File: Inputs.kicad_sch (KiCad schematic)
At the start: 5 parts, among them J401 inputs, J402 inputs, J403 common, U401 MCP23017_SP

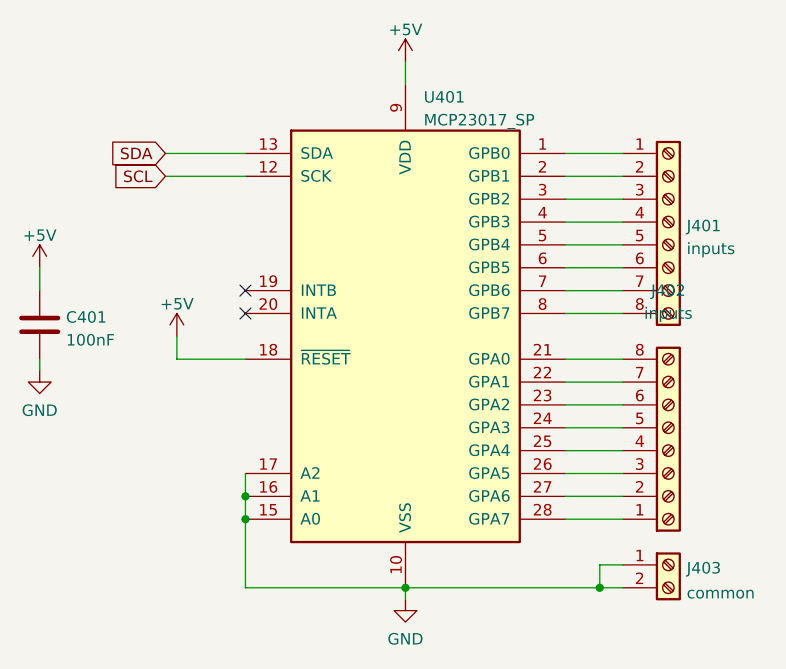
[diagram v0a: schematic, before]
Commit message: added something to debug the channel buttons
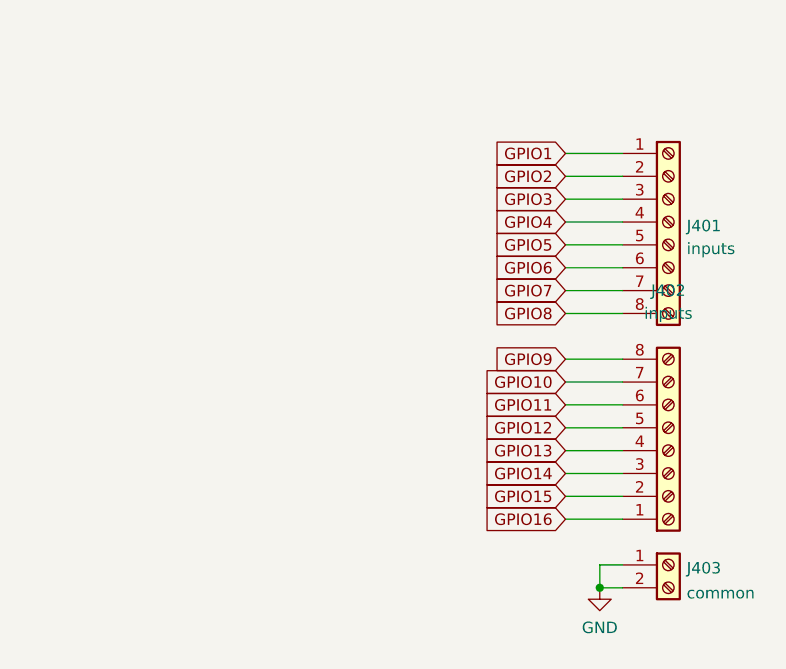
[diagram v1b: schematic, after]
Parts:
- removed C401: 100nF, Capacitor_THT:C_Disc_D3.0mm_W1.6mm_P2.50mm, symbol Device:C
- removed U401: MCP23017_SP, Package_DIP:DIP-28_W7.62mm_Socket, symbol Interface_Expansion:MCP23017_SP
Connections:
- net GPIO1: now reaches J401.1 (Pin_1)
- net GPIO2: now reaches J401.2 (Pin_2)
- net GPIO3: now reaches J401.3 (Pin_3)
- net GPIO4: now reaches J401.4 (Pin_4)
- net GPIO5: now reaches J401.5 (Pin_5)
- net GPIO6: now reaches J401.6 (Pin_6)
- net GPIO7: now reaches J401.7 (Pin_7)
- net GPIO8: now reaches J401.8 (Pin_8)
- net GPIO16: now reaches J402.1 (Pin_1)
- net GPIO15: now reaches J402.2 (Pin_2)
- net GPIO14: now reaches J402.3 (Pin_3)
- net GPIO13: now reaches J402.4 (Pin_4)
- net GPIO12: now reaches J402.5 (Pin_5)
- net GPIO11: now reaches J402.6 (Pin_6)
- net GPIO10: now reaches J402.7 (Pin_7)
- net GPIO9: now reaches J402.8 (Pin_8)
- no-connect marks 2 -> 0
